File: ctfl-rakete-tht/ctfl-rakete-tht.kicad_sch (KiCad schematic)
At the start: 0 parts

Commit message: added symbols for battery clip, ATtiny, power switch and one LED
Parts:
- added BT1: CR2032, Battery:BatteryHolder_Multicomp_BC-2001_1x2032, symbol Device:Battery_Cell
- added D1: LED_WarmWhite, LED_SMD:LED_0805_2012Metric_Pad1.15x1.40mm_HandSolder, symbol Device:LED_Small
- added SW1: SW_SPDT, Button_Switch_SMD:SW_SPDT_CK_JS102011SAQN, symbol Switch:SW_SPDT
- added U1: ATtiny85-20S, Package_SO:SOIC-8W_5.3x5.3mm_P1.27mm, symbol MCU_Microchip_ATtiny:ATtiny85-20S

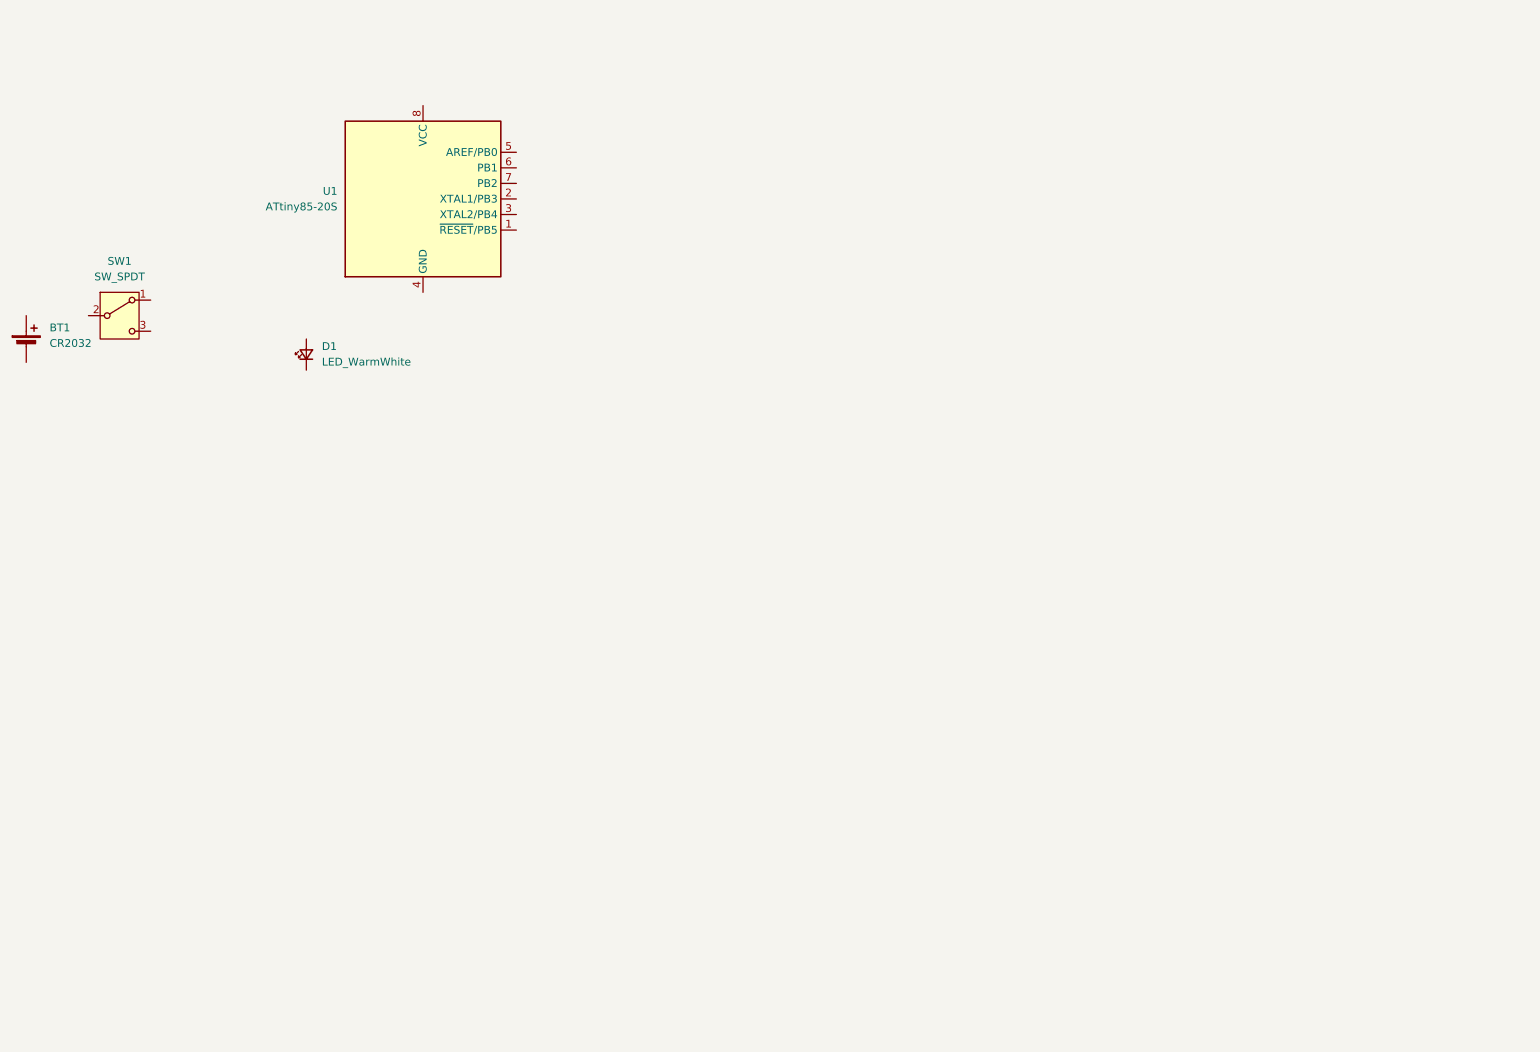
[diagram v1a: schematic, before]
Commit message: added LED symbols and a bunch of wires and replaced ATTINY85 with ATTINY212 symbol
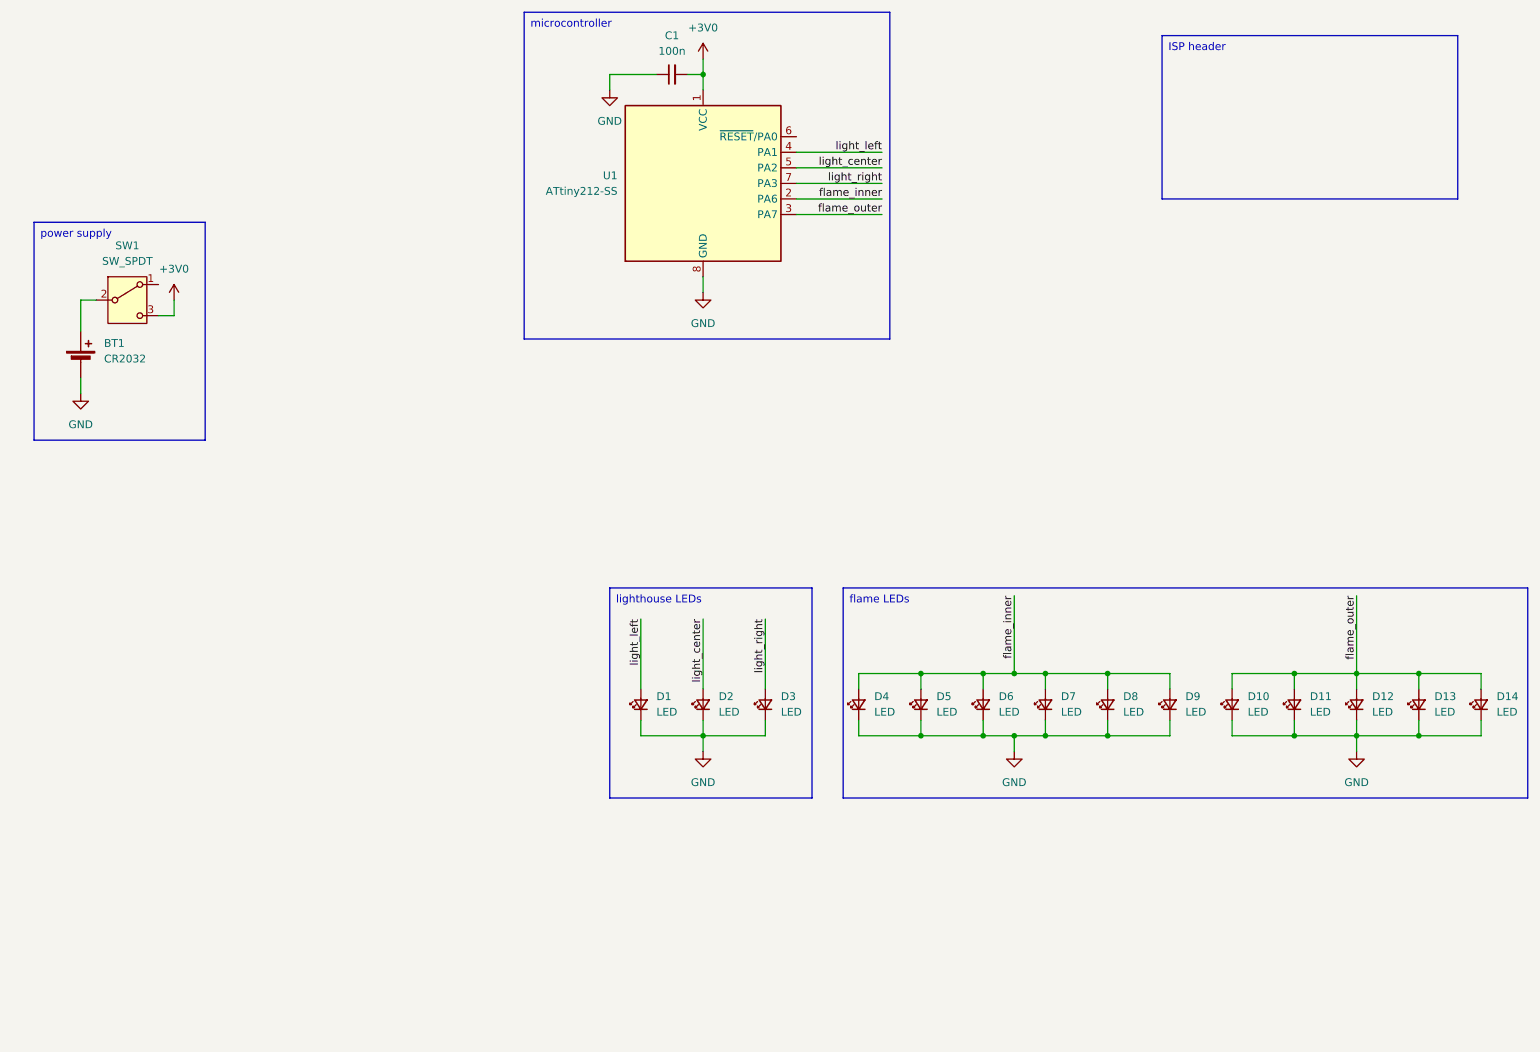
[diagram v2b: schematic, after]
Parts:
- removed U1: ATtiny85-20S, Package_SO:SOIC-8W_5.3x5.3mm_P1.27mm, symbol MCU_Microchip_ATtiny:ATtiny85-20S
- added C1: 100n, symbol Device:C_Small
- added D10, D11, D12, D13, D14, D2, D3, D4, D5, D6, D7, D8, D9: LED, local:LED_combo_0805_5mmSMD_HandSolder, symbol Device:LED_Small
- added U1: ATtiny212-SS, Package_SO:SOIC-8_3.9x4.9mm_P1.27mm, symbol MCU_Microchip_ATtiny:ATtiny212-SS
- D1: value LED_WarmWhite -> LED; footprint LED_SMD:LED_0805_2012Metric_Pad1.15x1.40mm_HandSolder -> local:LED_combo_0805_5mmSMD_HandSolder
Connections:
- net at BT1.1 (+): now also SW1.2 (B)
- net GND: now reaches BT1.2 (-)
- net GND: now also D1.1 (K), C1.1, D10.1 (K), D11.1 (K), D12.1 (K), D13.1 (K), D14.1 (K), D2.1 (K), D3.1 (K), D4.1 (K), D5.1 (K), D6.1 (K), D7.1 (K), D8.1 (K), D9.1 (K), U1.8 (GND)
- net +3V0: now reaches SW1.3 (C)
- net +3V0: now also C1.2, U1.1 (VCC)
- net light_left: now reaches D1.2 (A)
- net light_left: now also U1.4 (PA1)
- new net flame_inner: D4.2 (A), D5.2 (A), D6.2 (A), D7.2 (A), D8.2 (A), D9.2 (A), U1.2 (PA6)
- new net flame_outer: D10.2 (A), D11.2 (A), D12.2 (A), D13.2 (A), D14.2 (A), U1.3 (PA7)
- new net light_center: D2.2 (A), U1.5 (PA2)
- new net light_right: D3.2 (A), U1.7 (PA3)
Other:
- moved on the sheet: BT1, D1, SW1

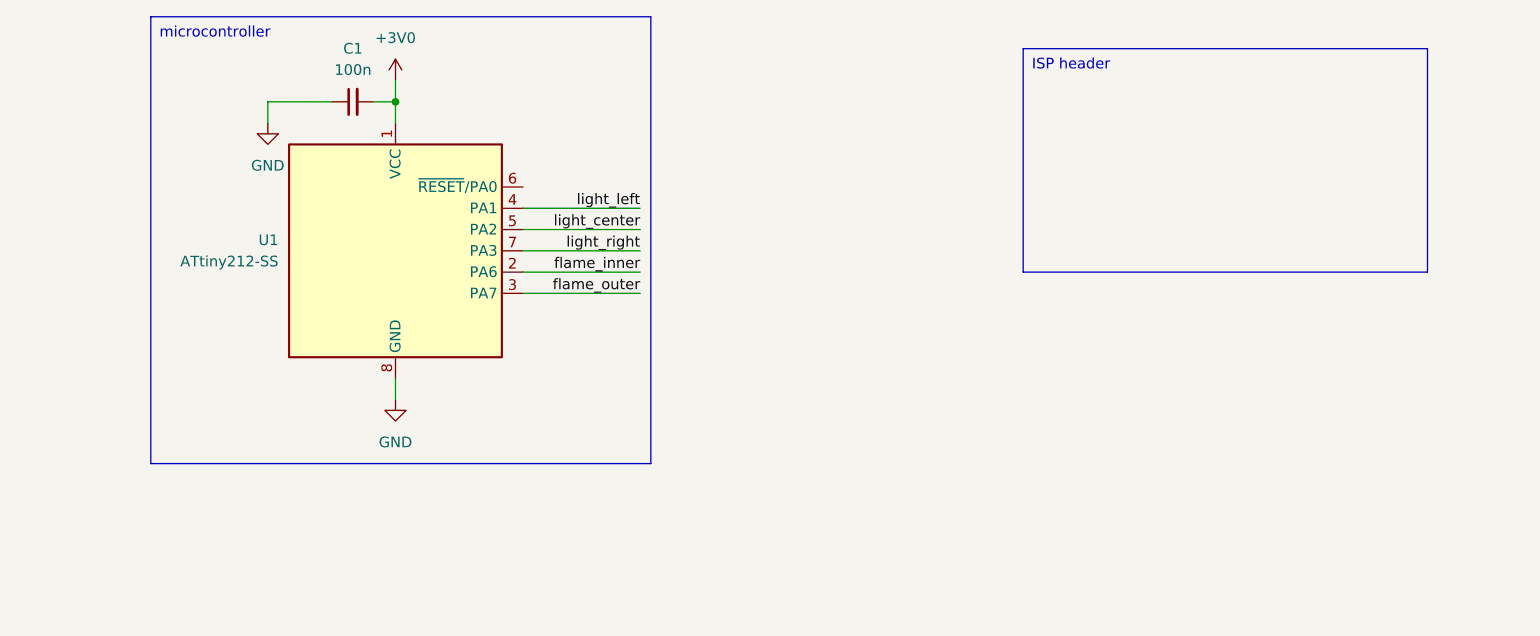
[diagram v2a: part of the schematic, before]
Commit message: added UPDI header and associated R and C
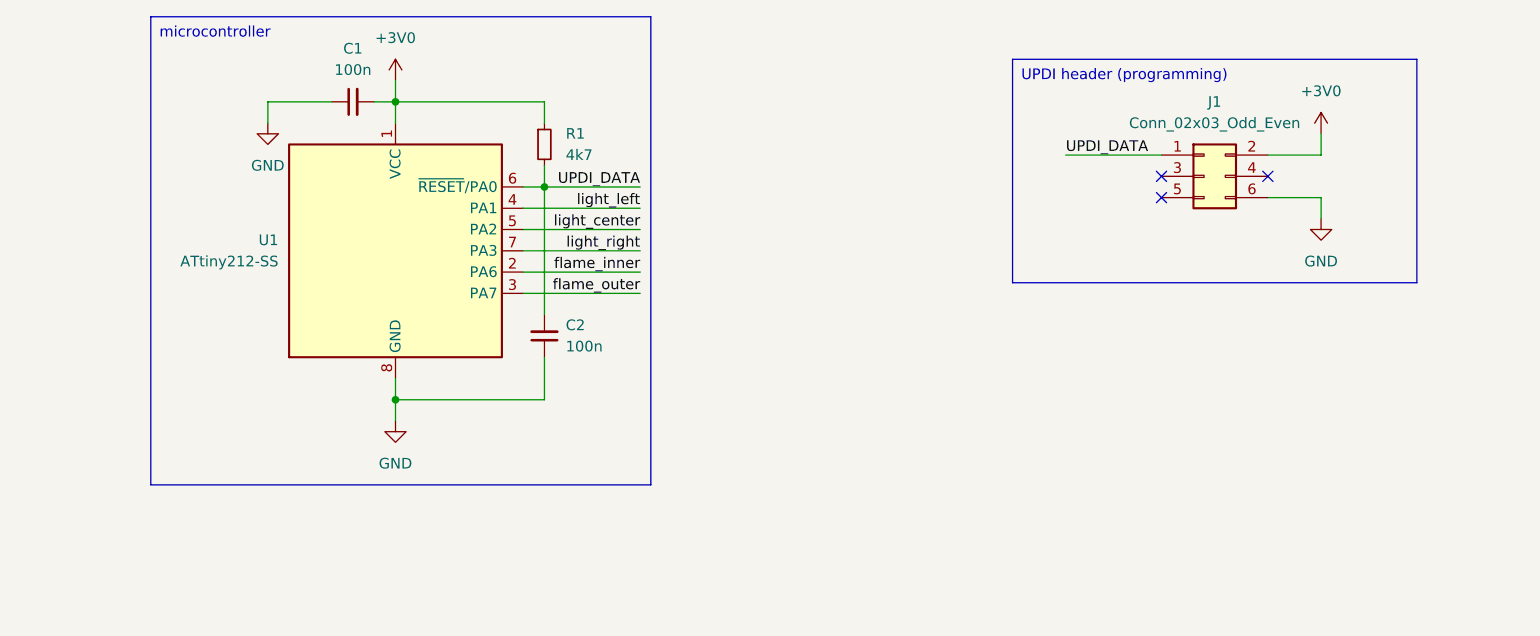
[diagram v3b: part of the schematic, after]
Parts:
- added C2: 100n, Capacitor_SMD:C_0805_2012Metric_Pad1.18x1.45mm_HandSolder, symbol Device:C_Small
- added J1: Conn_02x03_Odd_Even, Connector_PinHeader_2.54mm:PinHeader_2x03_P2.54mm_Vertical_SMD, symbol Connector_Generic:Conn_02x03_Odd_Even
- added R1: 4k7, Resistor_SMD:R_0805_2012Metric_Pad1.20x1.40mm_HandSolder, symbol Device:R_Small
- C1: footprint (none) -> Capacitor_SMD:C_0805_2012Metric_Pad1.18x1.45mm_HandSolder
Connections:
- net +3V0: now also J1.2 (Pin_2), R1.1
- net GND: now also C2.1, J1.6 (Pin_6)
- net UPDI_DATA: now reaches U1.6 (~{RESET}/PA0)
- net UPDI_DATA: now also C2.2, J1.1 (Pin_1), R1.2
- no-connect marks 0 -> 3

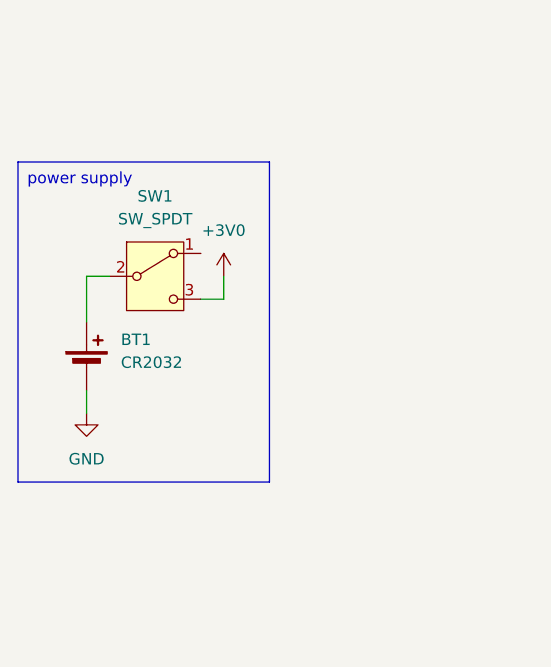
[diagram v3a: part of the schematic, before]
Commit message: added pwr_flags to satisfy ERC in schematic
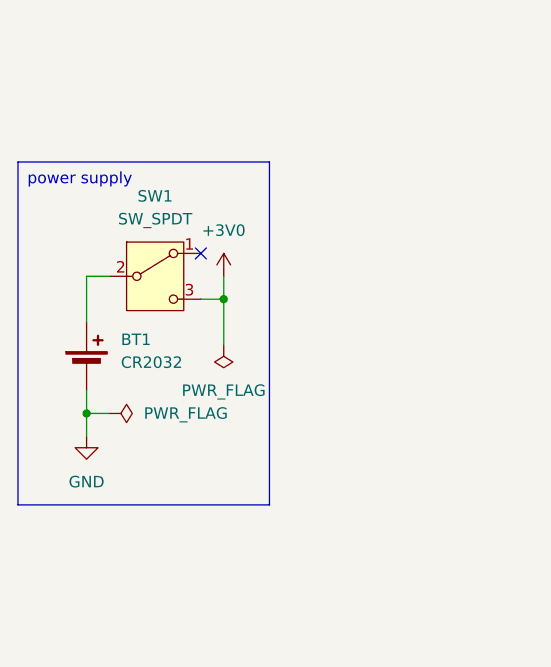
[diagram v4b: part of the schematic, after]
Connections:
- no-connect marks 3 -> 4
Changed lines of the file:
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@@
 	)
 	(junction
+		(at 38.1 82.55)
+		(diameter 0)
+		(color 0 0 0 0)
+	)
+	(junction
 		(at 139.7 66.04)
 		(diameter 0)
@@
 	)
 	(junction
+		(at 53.34 69.85)
+		(diameter 0)
+		(color 0 0 0 0)
+	)
+	(junction
 		(at 175.26 128.27)
 		(diameter 0)
@@
 		(at 231.14 39.37)
 	)
+	(no_connect
+		(at 50.8 64.77)
+	)
 	(wire
 		(pts
@@
 	(wire
 		(pts
+			(xy 53.34 69.85) (xy 53.34 74.93)
+		)
+		(stroke
+			(width 0)
+			(type default)
+		)
+	)
+	(wire
+		(pts
 			(xy 154.94 45.72) (xy 168.91 45.72)
 		)
@@
 	(wire
 		(pts
+			(xy 38.1 82.55) (xy 40.64 82.55)
+		)
+		(stroke
+			(width 0)
+			(type default)
+		)
+	)
+	(wire
+		(pts
+			(xy 38.1 82.55) (xy 38.1 85.09)
+		)
+		(stroke
+			(width 0)
+			(type default)
+		)
+	)
+	(wire
+		(pts
 			(xy 215.9 128.27) (xy 215.9 130.81)
 		)
@@
 		(exclude_from_sim no)
 		(at 30.48 54.61 0)
-		(size 27.94 35.56)
+		(size 27.94 38.1)
 		(stroke
 			(width 0)
@@
 	)
 	(symbol
+		(lib_id "power:PWR_FLAG")
+		(at 53.34 74.93 180)
+		(unit 1)
+		(exclude_from_sim no)
+		(in_bom yes)
+		(on_board yes)
+		(dnp no)
+		(fields_autoplaced yes)
+		(property "Reference" "#FLG01"
+			(at 53.34 76.835 0)
+			(effects
+				(font
+					(size 1.27 1.27)
+				)
+				(hide yes)
+			)
+		)
+		(property "Value" "PWR_FLAG"
+			(at 53.34 80.01 0)
+			(effects
+				(font
+					(size 1.27 1.27)
+				)
+			)
+		)
+		(property "Footprint" ""
+			(at 53.34 74.93 0)
+			(effects
+				(font
+					(size 1.27 1.27)
+				)
+				(hide yes)
+			)
+		)
+		(property "Datasheet" "~"
+			(at 53.34 74.93 0)
+			(effects
+				(font
+					(size 1.27 1.27)
+				)
+				(hide yes)
+			)
+		)
+		(property "Description" "Special symbol for telling ERC where power comes from"
+			(at 53.34 74.93 0)
+			(effects
+				(font
+					(size 1.27 1.27)
+				)
+				(hide yes)
+			)
+		)
+		(pin "1"
+		)
+		(instances
+			(project "ctfl-rakete-tht"
+				(path "/829bb9b1-d184-4115-9887-268f3090b165"
+					(reference "#FLG01")
+					(unit 1)
+				)
+			)
+		)
+	)
+	(symbol
 		(lib_id "Device:LED_Small")
 		(at 266.7 133.35 90)
@@
 	(symbol
 		(lib_id "power:GND")
-		(at 38.1 82.55 0)
+		(at 38.1 85.09 0)
 		(unit 1)
 		(exclude_from_sim no)
@@
 		(fields_autoplaced yes)
 		(property "Reference" "#PWR01"
-			(at 38.1 88.9 0)
+			(at 38.1 91.44 0)
 			(effects
 				(font
@@
 		)
 		(property "Value" "GND"
-			(at 38.1 87.63 0)
+			(at 38.1 90.17 0)
 			(effects
 				(font
@@
 		)
 		(property "Footprint" ""
-			(at 38.1 82.55 0)
+			(at 38.1 85.09 0)
 			(effects
 				(font
@@
 		)
 		(property "Datasheet" ""
-			(at 38.1 82.55 0)
+			(at 38.1 85.09 0)
 			(effects
 				(font
@@
 		)
 		(property "Description" "Power symbol creates a global label with name \"GND\" , ground"
-			(at 38.1 82.55 0)
+			(at 38.1 85.09 0)
 			(effects
 				(font
@@
 					(unit 1)
 				)
+			)
+		)
+	)
+	(symbol
+		(lib_id "power:PWR_FLAG")
+		(at 40.64 82.55 270)
+		(unit 1)
+		(exclude_from_sim no)
+		(in_bom yes)
+		(on_board yes)
+		(dnp no)
+		(fields_autoplaced yes)
+		(property "Reference" "#FLG02"
+			(at 42.545 82.55 0)
+			(effects
+				(font
+					(size 1.27 1.27)
+				)
+				(hide yes)
+			)
+		)
+		(property "Value" "PWR_FLAG"
+			(at 44.45 82.5499 90)
+			(effects
+				(font
+					(size 1.27 1.27)
+				)
+				(justify left)
+			)
+		)
+		(property "Footprint" ""
+			(at 40.64 82.55 0)
+			(effects
+				(font
+					(size 1.27 1.27)
+				)
+				(hide yes)
+			)
+		)
+		(property "Datasheet" "~"
+			(at 40.64 82.55 0)
+			(effects
+				(font
+					(size 1.27 1.27)
+				)
+				(hide yes)
+			)
+		)
+		(property "Description" "Special symbol for telling ERC where power comes from"
+			(at 40.64 82.55 0)
+			(effects
+				(font
+					(size 1.27 1.27)
+				)
+				(hide yes)
+			)
+		)
+		(pin "1"
+		)
+		(instances
+			(project "ctfl-rakete-tht"
+				(path "/829bb9b1-d184-4115-9887-268f3090b165"
+					(reference "#FLG02")
+					(unit 1)
+				)

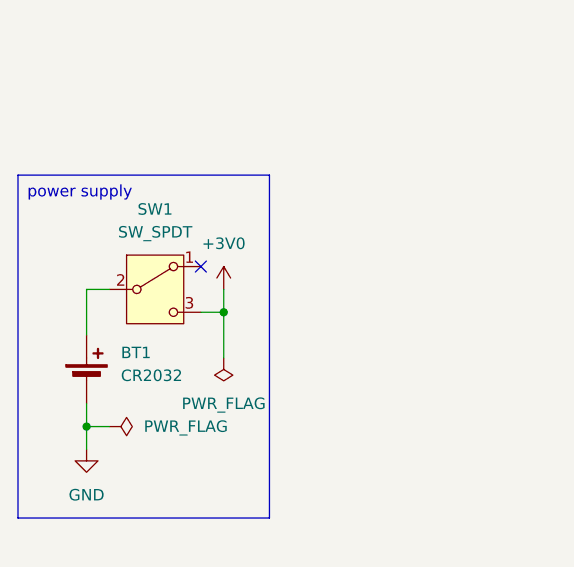
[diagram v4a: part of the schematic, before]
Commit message: optimized switch connections
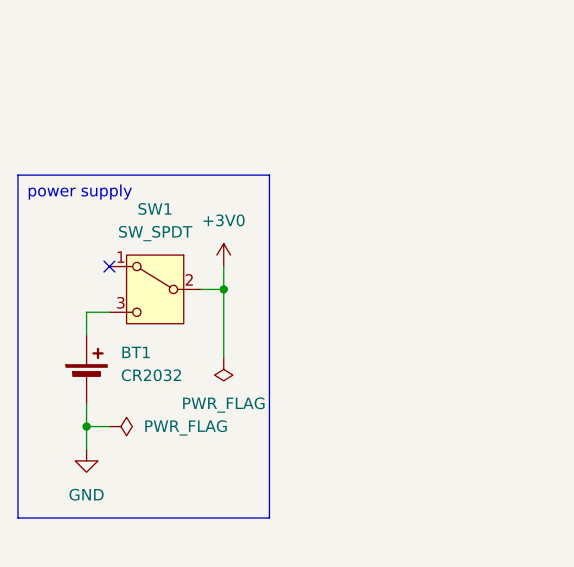
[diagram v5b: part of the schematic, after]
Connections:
- net +3V0: now also SW1.2 (B); no longer SW1.3 (C)
- net at BT1.1 (+): now also SW1.3 (C); no longer SW1.2 (B)
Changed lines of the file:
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@@
-	)
-	(junction
-		(at 53.34 69.85)
-		(diameter 0)
-		(color 0 0 0 0)
 	)
 	(junction
@@
 		(color 0 0 0 0)
 	)
+	(junction
+		(at 53.34 67.31)
+		(diameter 0)
+		(color 0 0 0 0)
+	)
 	(no_connect
 		(at 243.84 39.37)
@@
 	)
 	(no_connect
-		(at 50.8 64.77)
+		(at 40.64 64.77)
 	)
 	(wire
@@
 	(wire
 		(pts
-			(xy 38.1 67.31) (xy 40.64 67.31)
+			(xy 38.1 69.85) (xy 40.64 69.85)
 		)
 		(stroke
@@
 	(wire
 		(pts
-			(xy 53.34 69.85) (xy 53.34 74.93)
-		)
-		(stroke
-			(width 0)
-			(type default)
-		)
-	)
-	(wire
-		(pts
 			(xy 154.94 45.72) (xy 168.91 45.72)
 		)
@@
 	(wire
 		(pts
-			(xy 50.8 69.85) (xy 53.34 69.85)
+			(xy 50.8 67.31) (xy 53.34 67.31)
 		)
 		(stroke
@@
 	(wire
 		(pts
-			(xy 53.34 69.85) (xy 53.34 67.31)
+			(xy 53.34 67.31) (xy 53.34 74.93)
 		)
 		(stroke
@@
 	(wire
 		(pts
+			(xy 53.34 67.31) (xy 53.34 64.77)
+		)
+		(stroke
+			(width 0)
+			(type default)
+		)
+	)
+	(wire
+		(pts
 			(xy 219.71 36.83) (xy 231.14 36.83)
 		)
@@
 	(wire
 		(pts
-			(xy 38.1 72.39) (xy 38.1 67.31)
+			(xy 38.1 72.39) (xy 38.1 69.85)
 		)
 		(stroke
@@
 		(lib_id "Switch:SW_SPDT")
 		(at 45.72 67.31 0)
+		(mirror y)
 		(unit 1)
 		(exclude_from_sim no)
@@
 		(on_board yes)
 		(dnp no)
-		(fields_autoplaced yes)
 		(property "Reference" "SW1"
 			(at 45.72 58.42 0)
@@
 	(symbol
 		(lib_id "power:+3V0")
-		(at 53.34 67.31 0)
+		(at 53.34 64.77 0)
 		(unit 1)
 		(exclude_from_sim no)
@@
 		(fields_autoplaced yes)
 		(property "Reference" "#PWR02"
-			(at 53.34 71.12 0)
+			(at 53.34 68.58 0)
 			(effects
 				(font
@@
 		)
 		(property "Value" "+3V0"
-			(at 53.34 62.23 0)
+			(at 53.34 59.69 0)
 			(effects
 				(font
@@
 		)
 		(property "Footprint" ""
-			(at 53.34 67.31 0)
+			(at 53.34 64.77 0)
 			(effects
 				(font
@@
 		)
 		(property "Datasheet" ""
-			(at 53.34 67.31 0)
+			(at 53.34 64.77 0)
 			(effects
 				(font
@@
 		)
 		(property "Description" "Power symbol creates a global label with name \"+3V0\""
-			(at 53.34 67.31 0)
-			(effects
-				(font
+			(at 53.34 64.77 0)
+			(effects
+				(font
